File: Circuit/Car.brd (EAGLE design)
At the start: 75.9 x 72.1 mm, 16 parts, among them M1 MOTOR, M2 MOTOR, U1 AMS1117-3.3, X2 ESP-12

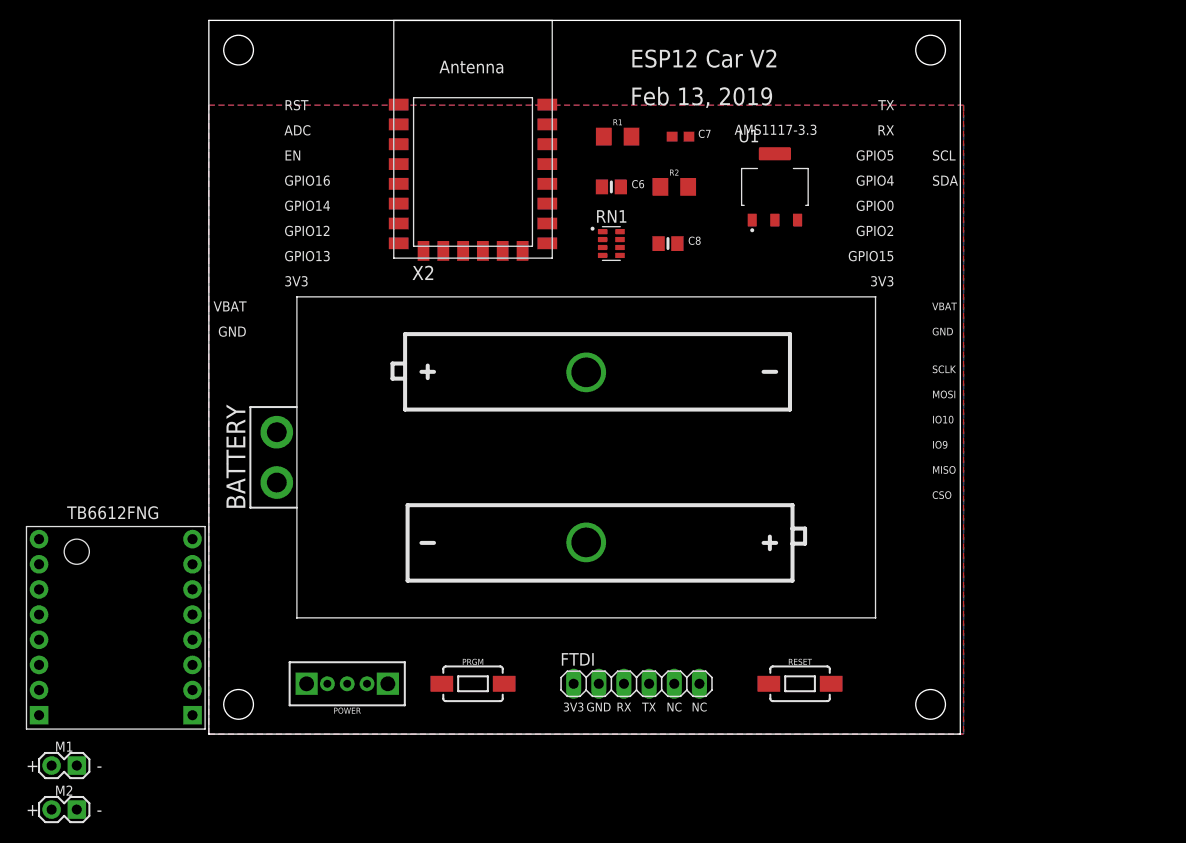
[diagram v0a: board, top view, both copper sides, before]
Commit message: update library, car PCB V2
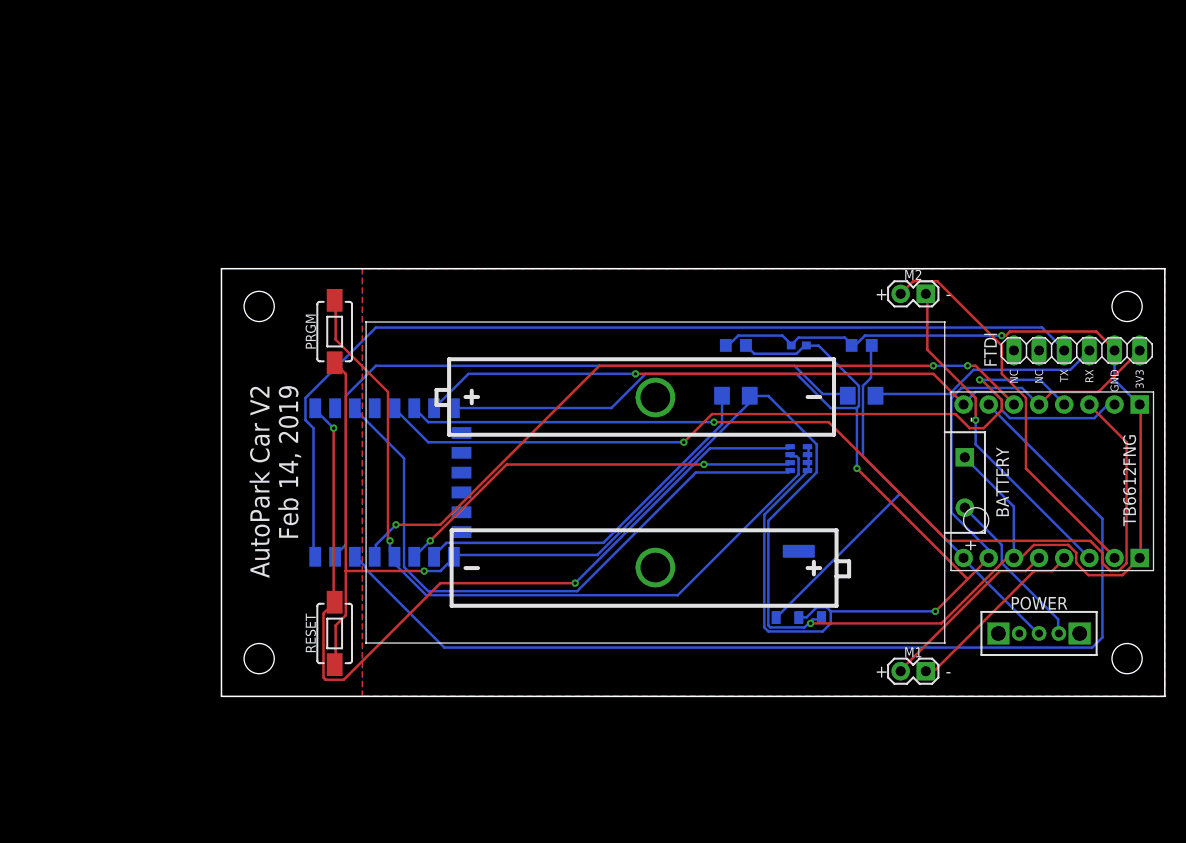
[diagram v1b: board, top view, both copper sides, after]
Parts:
- C6, C8: device microbuilder:0805-NO -> AutoPark:MICROBUILDER__0805
- C7: device microbuilder:0603-NO -> AutoPark:MICROBUILDER__0603
- POWER: value SWITCH_SPDT_SLIDE -> Switch
- moved M2 100.3 mm to (69.8, 44.5)
- moved TB1 92.9 mm to (82.5, 25.4), turned to 90 degrees
- moved M1 86.3 mm to (69.8, 6.35)
- moved POWER 70.0 mm to (83.8, 10.2), turned to 270 degrees
- moved FTDI 55.8 mm to (87.6, 38.7), turned to 180 degrees
- moved RESET 47.3 mm to (12.7, 10.2), turned to 90 degrees
- moved U1 40.2 mm to (59.6, 15.1), flipped to the bottom
- moved PRGM 38.2 mm to (12.7, 40.6), turned to 90 degrees
- moved R1 35.9 mm to (65.9, 34.2), flipped to the bottom
- moved X2 33.9 mm to (16.5, 25.4), flipped to the bottom, turned to 270 degrees
- moved C6 29.9 mm to (65.9, 39.2), flipped to the bottom
- moved RN1 28.8 mm to (59.6, 27.8), flipped to the bottom
- moved C7 24.2 mm to (59.6, 39.2), flipped to the bottom
- moved R2 22.0 mm to (53.2, 34.2), flipped to the bottom
- moved C8 12.4 mm to (53.2, 39.2), flipped to the bottom
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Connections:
- net GPIO13/MOSI: now also TB1.PWMB
- net GPIO16: no longer TB1.PWMB
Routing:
- net GND: track 0.00 -> 231.2 mm, vias 0 -> 3
- net 3.3V: track 0.00 -> 172.5 mm, vias 0 -> 2
- net GPIO5/SCL: track 0.00 -> 108.1 mm
- net GPIO12/MISO: track 0.00 -> 97.2 mm, vias 0 -> 1
- net TXD: track 0.00 -> 97.0 mm
- net RESET: track 0.00 -> 85.4 mm, vias 0 -> 2
- net GPIO0: track 0.00 -> 79.0 mm, vias 0 -> 1
- net GPIO14/SCK: track 0.00 -> 79.0 mm, vias 0 -> 2
- net GPIO4/SDA: track 0.00 -> 74.8 mm, vias 0 -> 3
- net GPIO13/MOSI: track 0.00 -> 74.4 mm, vias 0 -> 1
- net RXD: track 0.00 -> 69.9 mm
- net CH_PD: track 0.00 -> 63.1 mm
- net VBAT: track 0.00 -> 54.7 mm
- net GPIO2: track 0.00 -> 41.9 mm, vias 0 -> 2
- net B1: track 0.00 -> 39.6 mm
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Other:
- board size 75.9 x 72.1 mm -> 95.2 x 43.2 mm
- board text added: "AutoPark Car V2 Feb 14, 2019"
- board text removed: "ADC"
- board text removed: "CSO"
- board text removed: "EN"
- board text removed: "ESP12 Car V2"
- board text removed: "Feb 13, 2019"
- board text removed: "GPIO0"
- board text removed: "GPIO12"
- board text removed: "GPIO13"
- board text removed: "GPIO14"
- board text removed: "GPIO15"
- board text removed: "GPIO16"
- board text removed: "GPIO2"
- board text removed: "GPIO4"
- board text removed: "GPIO5"
- board text removed: "IO10"
- board text removed: "IO9"
- board text removed: "MISO"
- board text removed: "MOSI"
- board text removed: "RST"
- board text removed: "SCL"
- board text removed: "SCLK"
- board text removed: "SDA"
- board text removed: "VBAT"

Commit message: car v3 with RGB, update platformio ESP dev structure
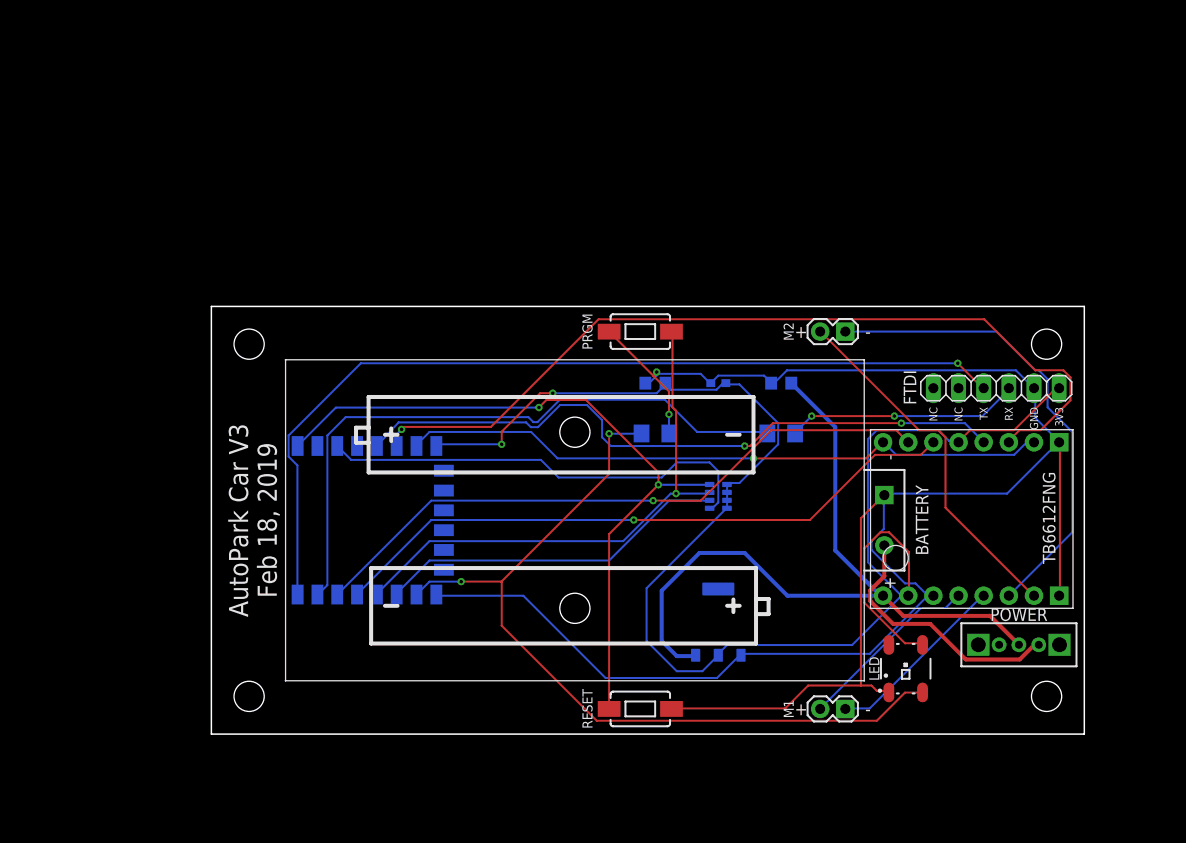
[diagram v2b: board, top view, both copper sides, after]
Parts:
- added LED: WS2812, AutoPark:LED-TRICOLOR-5050-IC
- moved RESET 31.8 mm to (43.6, 2.54), turned to 180 degrees
- moved PRGM 30.9 mm to (43.6, 40.6), turned to 0 degrees
- moved BATTERY 8.98 mm to (37.0, 21.6)
- moved C6 8.98 mm to (57.8, 35.4)
- moved C7 8.98 mm to (51.4, 35.4)
- moved C8 8.98 mm to (45.1, 35.4)
- moved FTDI 8.98 mm to (79.5, 34.9)
- moved RN1 8.98 mm to (51.4, 24.0)
- moved TB1 8.98 mm to (74.4, 21.6)
- moved U1 8.98 mm to (51.4, 11.3)
- moved R1 8.98 mm to (57.8, 30.4)
- moved R2 8.98 mm to (45.1, 30.4)
- moved M2 8.98 mm to (61.7, 40.6)
- moved M1 8.98 mm to (61.7, 2.54)
- moved X2 4.20 mm to (14.7, 21.6)
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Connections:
- net 3.3V: now also LED.VDD
- net GND: now also LED.VSS
- net GPIO15: now also LED.DIN
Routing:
- net GPIO15: track 37.6 -> 83.9 mm, vias 0 -> 2
- net GPIO5/SCL: track 108.1 -> 65.0 mm, vias 0 -> 1
- net GPIO0: track 79.0 -> 54.6 mm
- net VBAT: track 54.7 -> 76.1 mm
- net GND: track 231.2 -> 211.8 mm, vias 3 -> 2
- net CH_PD: track 63.1 -> 45.0 mm
- net B2: track 33.5 -> 48.0 mm, vias 1 -> 0
- net RESET: track 85.4 -> 72.5 mm
- net GPIO14/SCK: track 79.0 -> 67.9 mm
- net GPIO12/MISO: track 97.2 -> 86.8 mm
- net GPIO4/SDA: track 74.8 -> 64.6 mm, vias 3 -> 1
- net 3.3V: track 172.5 -> 162.7 mm
- net N$1: track 16.7 -> 26.3 mm
- net GPIO13/MOSI: track 74.4 -> 65.8 mm
- net TXD: track 97.0 -> 90.7 mm, vias 0 -> 1
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- removed copper zone on layer 1, net GND
- removed copper zone on layer 16, net GND
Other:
- board size 95.2 x 43.2 mm -> 88.1 x 43.2 mm
- board text added: "AutoPark Car V3 Feb 18, 2019"
- board text removed: "AutoPark Car V2 Feb 14, 2019"
